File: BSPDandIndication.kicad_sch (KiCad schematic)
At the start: 52 parts, among them J2 Masa, J3 12VTelem, J4 Sensors, J6 BSPD12OUT, K1 FINDER-36.11, Q1 BC817, U1 LM1117-5.0, U2 LM1117-5.0, U3 PIC12F629-IP, U4 LM324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

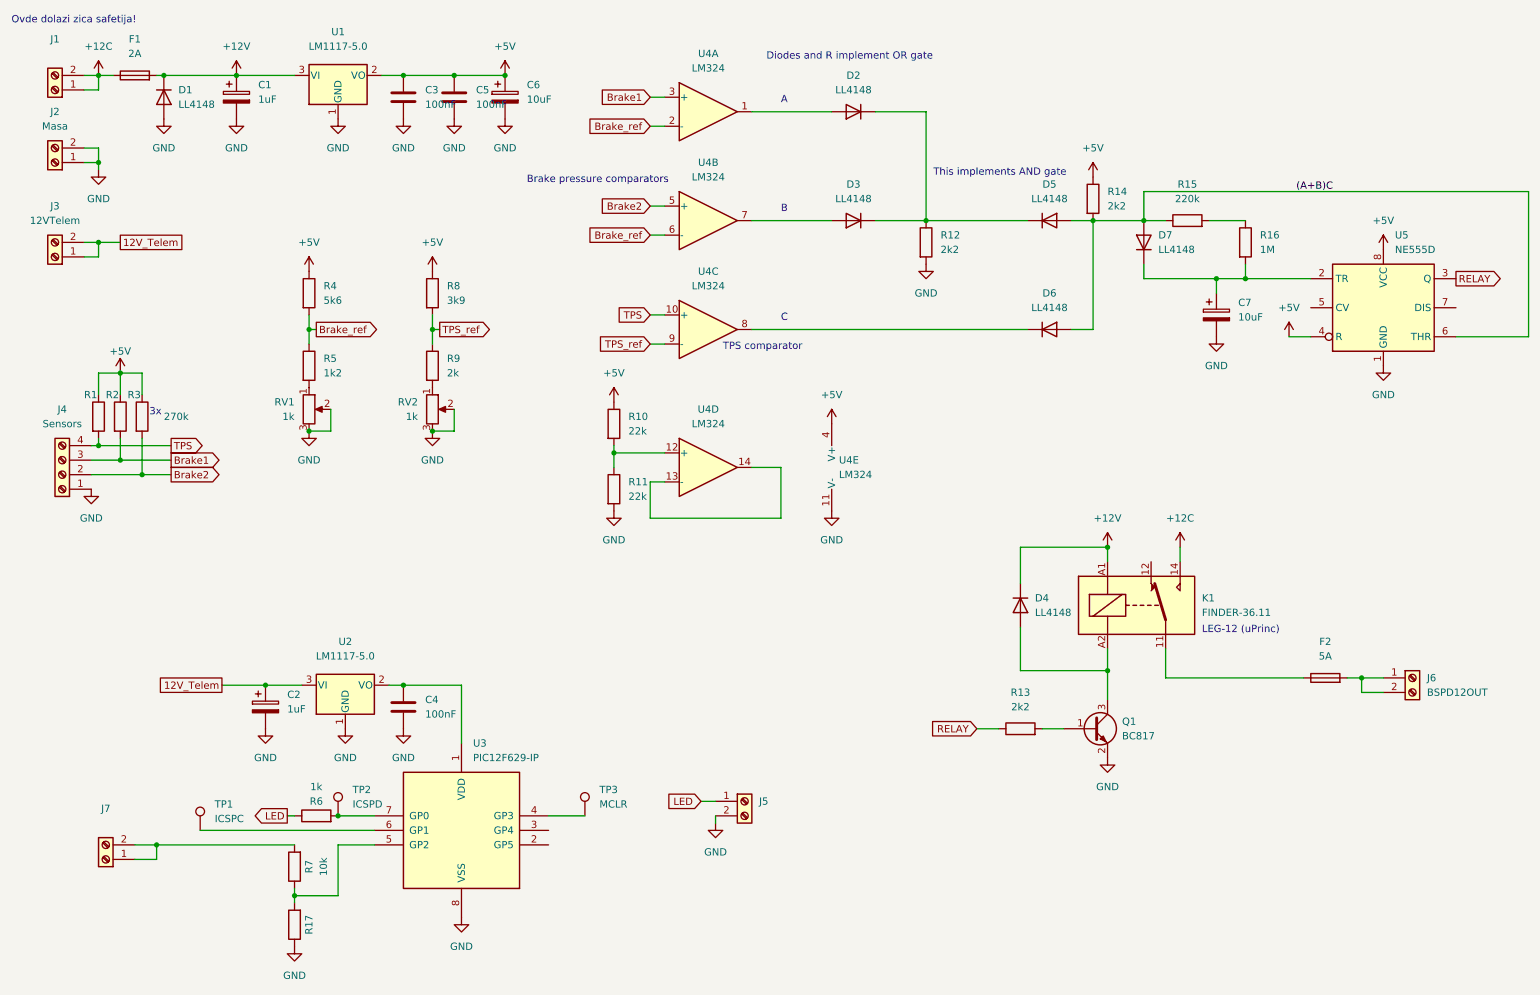
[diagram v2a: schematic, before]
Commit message: Only one fuse needed
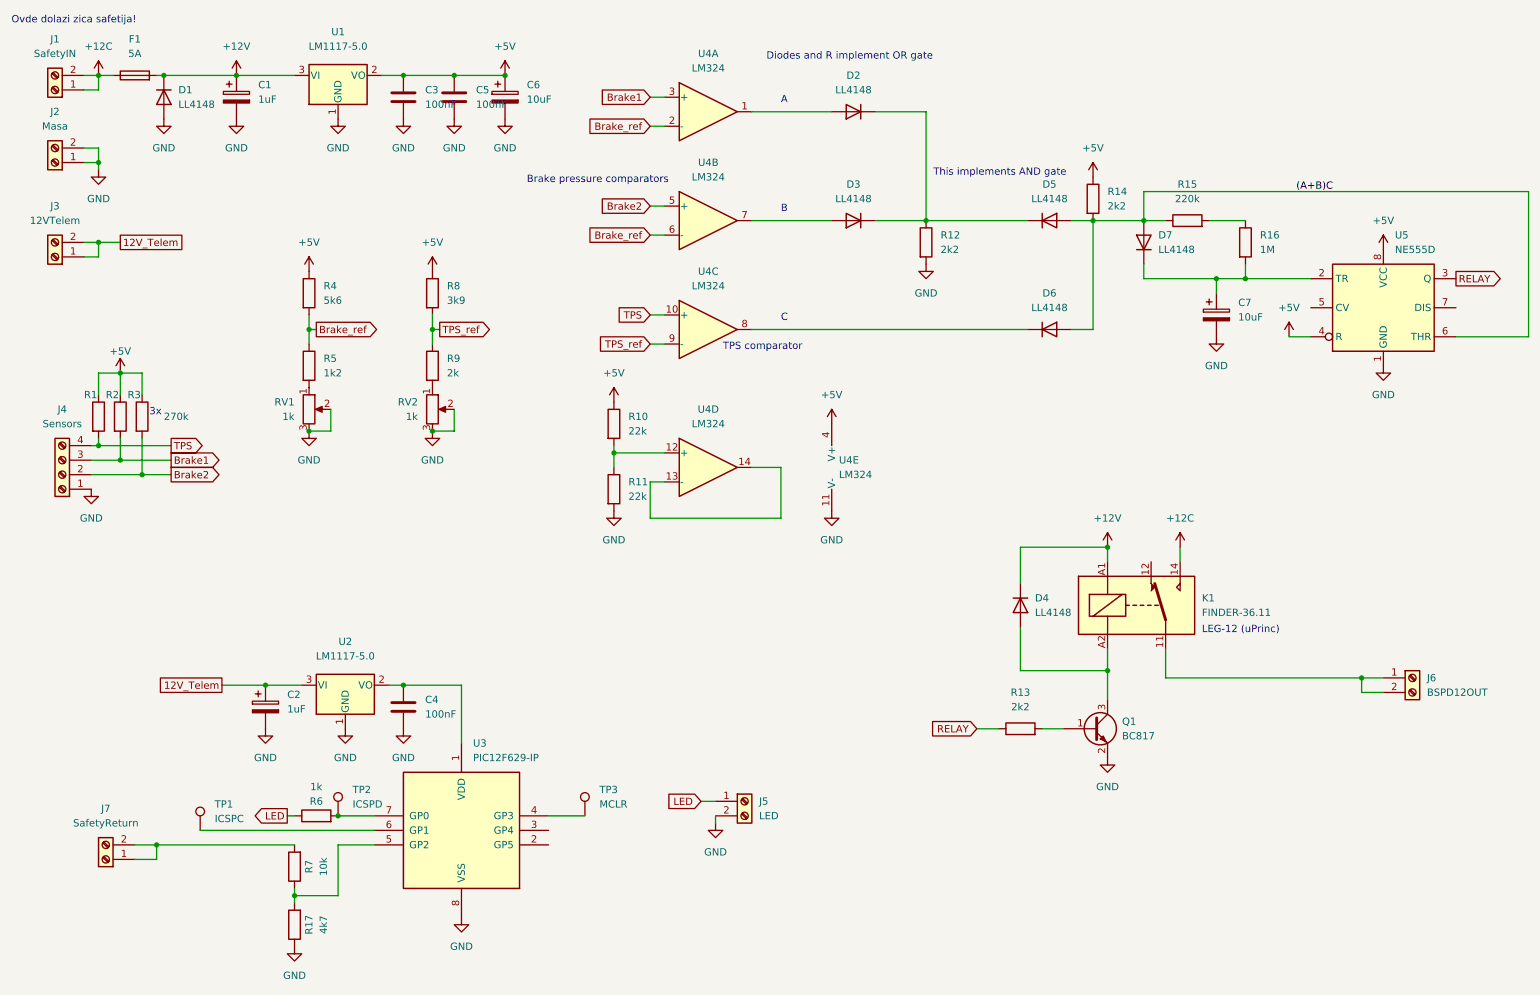
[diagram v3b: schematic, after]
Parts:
- removed F2: 5A, Fuse:Fuseholder_Cylinder-5x20mm_Schurter_0031_8201_Horizontal_Open, symbol Device:Fuse
- F1: value 2A -> 5A; footprint Fuse:Fuse_2512_6332Metric_Pad1.52x3.35mm_HandSolder -> Fuse:Fuseholder_Cylinder-5x20mm_Schurter_0031_8201_Horizontal_Open
- J1: value (none) -> SafetyIN
- J5: value (none) -> LED
- J7: value (none) -> SafetyReturn
- R17: value (none) -> 4k7
- U4: footprint (none) -> Package_SO:SO-14_3.9x8.65mm_P1.27mm
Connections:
- net at K1.11: now also J6.1 (Pin_1), J6.2 (Pin_2)
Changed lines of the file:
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@@
-    (stroke (width 0) (type default) (color 0 0 0 0))
-  )
-  (wire (pts (xy 241.3 130.81) (xy 217.17 130.81))
     (stroke (width 0) (type default) (color 0 0 0 0))
   )
@@
     (stroke (width 0) (type default) (color 0 0 0 0))
   )
-  (wire (pts (xy 248.92 130.81) (xy 251.46 130.81))
+  (wire (pts (xy 217.17 130.81) (xy 251.46 130.81))
     (stroke (width 0) (type default) (color 0 0 0 0))
   )
@@
     (pin "3")
   )
-  (symbol (lib_id "Device:Fuse") (at 245.11 130.81 90) (unit 1)
-    (in_bom yes) (on_board yes) (fields_autoplaced)
-    (property "Reference" "F2" (id 0) (at 245.11 124.46 90))
-    (property "Value" "5A" (id 1) (at 245.11 127 90))
-    (property "Footprint" "Fuse:Fuseholder_Cylinder-5x20mm_Schurter_0031_8201_Horizontal_Open" (id 2) (at 245.11 132.588 90)
-      (effects (font (size 1.27 1.27)) hide)
-    )
-    (property "Datasheet" "~" (id 3) (at 245.11 130.81 0)
-      (effects (font (size 1.27 1.27)) hide)
-    )
-    (pin "1")
-    (pin "2")
-  )
   (symbol (lib_id "power:GND") (at 138.43 156.21 0) (unit 1)
     (in_bom yes) (on_board yes) (fields_autoplaced)
@@
     (in_bom yes) (on_board yes) (fields_autoplaced)
     (property "Reference" "J1" (id 0) (at 22.86 19.05 0))
-    (property "Value" "" (id 1) (at 22.86 21.59 0))
+    (property "Value" "SafetyIN" (id 1) (at 22.86 21.59 0))
     (property "Footprint" "AK3001:AK300_1x02_P5.00mm_45-Degree" (id 2) (at 22.86 27.94 0)
       (effects (font (size 1.27 1.27)) hide)
@@
     (pin "2")
   )
-  (symbol (lib_id "Device:Fuse") (at 36.83 25.4 90) (unit 1)
-    (in_bom yes) (on_board yes) (fields_autoplaced)
-    (property "Reference" "F1" (id 0) (at 36.83 19.05 90))
-    (property "Value" "2A" (id 1) (at 36.83 21.59 90))
-    (property "Footprint" "Fuse:Fuse_2512_6332Metric_Pad1.52x3.35mm_HandSolder" (id 2) (at 36.83 27.178 90)
-      (effects (font (size 1.27 1.27)) hide)
-    )
-    (property "Datasheet" "~" (id 3) (at 36.83 25.4 0)
-      (effects (font (size 1.27 1.27)) hide)
-    )
-    (pin "1")
-    (pin "2")
-  )
   (symbol (lib_id "power:GND") (at 30.48 41.91 0) (unit 1)
     (in_bom yes) (on_board yes)
@@
       (effects (font (size 1.27 1.27)) (justify left))
     )
-    (property "Footprint" "" (id 2) (at 160.02 91.44 0)
+    (property "Footprint" "Package_SO:SO-14_3.9x8.65mm_P1.27mm" (id 2) (at 160.02 91.44 0)
       (effects (font (size 1.27 1.27)) hide)
     )
@@
     (in_bom yes) (on_board yes) (fields_autoplaced)
     (property "Reference" "J7" (id 0) (at 31.75 153.67 0))
-    (property "Value" "" (id 1) (at 31.75 156.21 0))
+    (property "Value" "SafetyReturn" (id 1) (at 31.75 156.21 0))
     (property "Footprint" "AK3001:AK300_1x02_P5.00mm_45-Degree" (id 2) (at 31.75 162.56 0)
       (effects (font (size 1.27 1.27)) hide)
@@
     )
     (property "Datasheet" "~" (id 3) (at 22.86 57.15 0)
+      (effects (font (size 1.27 1.27)) hide)
+    )
+    (pin "1")
+    (pin "2")
+  )
+  (symbol (lib_id "Device:Fuse") (at 36.83 25.4 90) (unit 1)
+    (in_bom yes) (on_board yes) (fields_autoplaced)
+    (property "Reference" "F1" (id 0) (at 36.83 19.05 90))
+    (property "Value" "5A" (id 1) (at 36.83 21.59 90))
+    (property "Footprint" "Fuse:Fuseholder_Cylinder-5x20mm_Schurter_0031_8201_Horizontal_Open" (id 2) (at 36.83 27.178 90)
+      (effects (font (size 1.27 1.27)) hide)
+    )
+    (property "Datasheet" "~" (id 3) (at 36.83 25.4 0)
       (effects (font (size 1.27 1.27)) hide)
     )
@@
     (in_bom yes) (on_board yes)
     (property "Reference" "R17" (id 0) (at 67.31 173.99 90))
-    (property "Value" "" (id 1) (at 69.85 173.99 90))
+    (property "Value" "4k7" (id 1) (at 69.85 173.99 90))
     (property "Footprint" "Resistor_SMD:R_1206_3216Metric_Pad1.30x1.75mm_HandSolder" (id 2) (at 66.548 173.99 90)
       (effects (font (size 1.27 1.27)) hide)
@@
       (effects (font (size 1.27 1.27)) (justify left))
     )
-    (property "Value" "" (id 1) (at 146.05 154.9399 0)
+    (property "Value" "LED" (id 1) (at 146.05 154.9399 0)
       (effects (font (size 1.27 1.27)) (justify left))
     )
@@
       (reference "D7") (unit 1) (value "LL4148") (footprint "Diode_SMD:D_MiniMELF")
     )
-    (path "/5fdea24e-408c-4aa0-856d-c76fa753c719"
-      (reference "F1") (unit 1) (value "2A") (footprint "Fuse:Fuse_2512_6332Metric_Pad1.52x3.35mm_HandSolder")
-    )
-    (path "/19f2bbdb-9b81-44ee-a59a-5a9297e7681f"
-      (reference "F2") (unit 1) (value "5A") (footprint "Fuse:Fuseholder_Cylinder-5x20mm_Schurter_0031_8201_Horizontal_Open")
+    (path "/b64d922b-f1cc-4940-96f6-60cbefb80766"
+      (reference "F1") (unit 1) (value "5A") (footprint "Fuse:Fuseholder_Cylinder-5x20mm_Schurter_0031_8201_Horizontal_Open")
     )
     (path "/539be303-c3c5-402b-99d9-cc01b8a3aa7c"
